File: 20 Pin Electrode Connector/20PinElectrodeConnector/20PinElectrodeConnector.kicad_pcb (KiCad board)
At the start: 2 copper layers, 21 parts, among them J1 Conn_02x10_Odd_Even

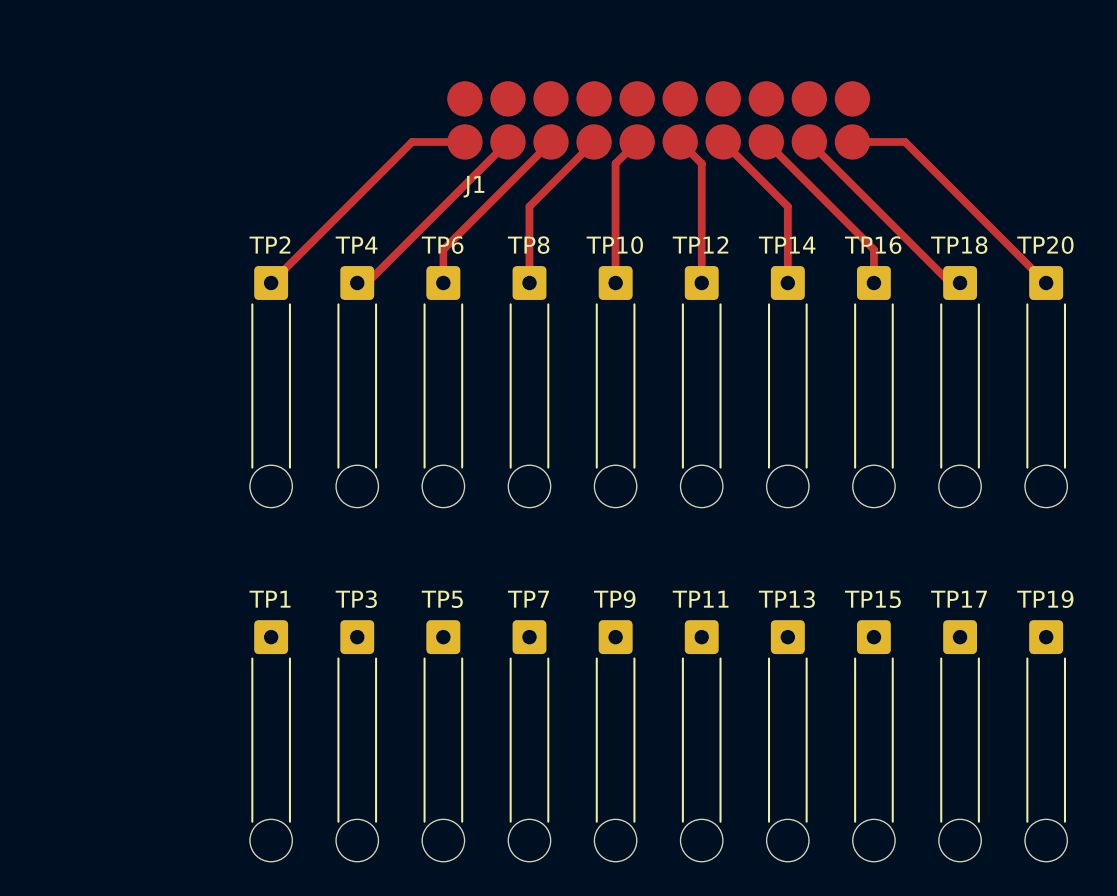
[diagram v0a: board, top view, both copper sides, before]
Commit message: Conform to microscope stage bracket.
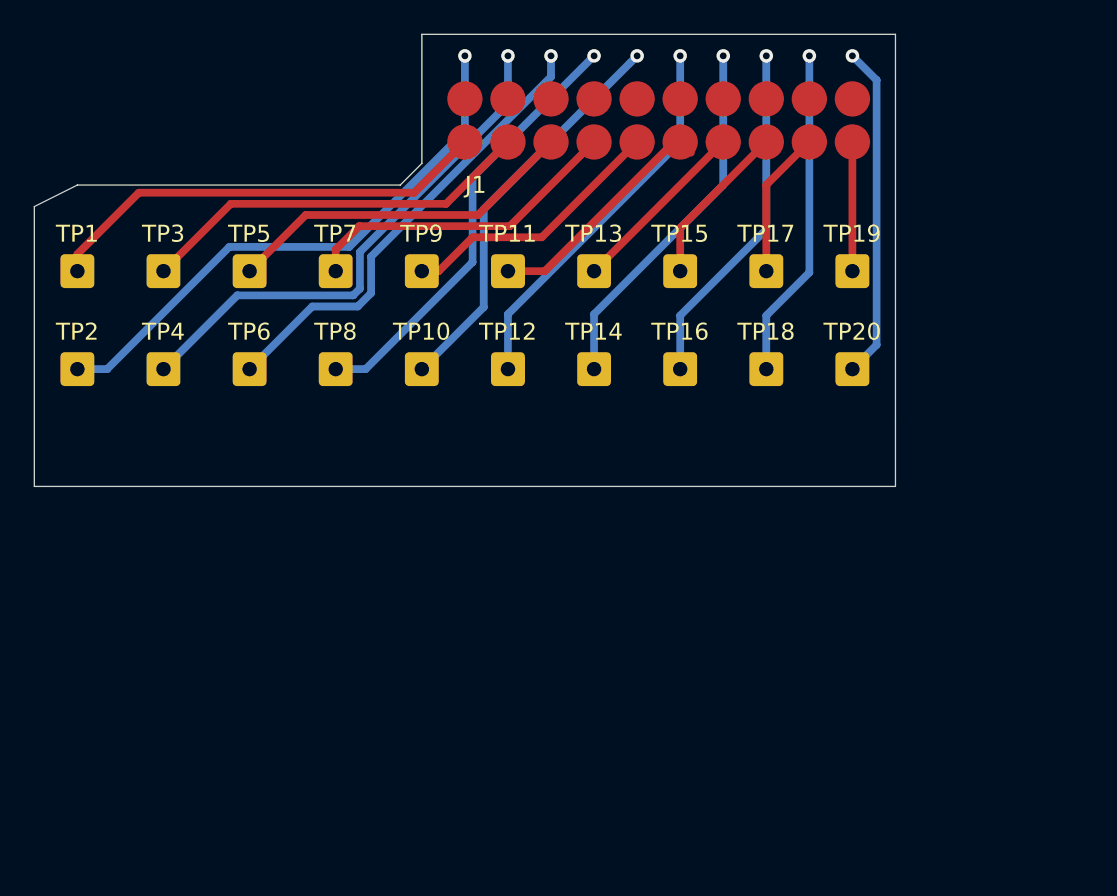
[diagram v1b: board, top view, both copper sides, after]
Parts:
- TP1, TP10, TP11, TP12, TP13, TP14, TP15, TP16, TP17, TP18, TP19, TP2, TP20, TP3, TP4, TP5, TP6, TP7, TP8, TP9: footprint Connector_Wire:SolderWire-0.25sqmm_1x01_D0.65mm_OD2mm_Relief -> Connector_Wire:SolderWire-0.25sqmm_1x01_D0.65mm_OD2mm
- moved TP11 24.4 mm to (114.3, 73.7)
- moved TP13 24.4 mm to (119.4, 73.7)
- moved TP17 24.4 mm to (129.5, 73.7)
- moved TP19 24.4 mm to (134.6, 73.7)
- moved TP9 24.4 mm to (109.2, 73.7)
- moved TP1 24.4 mm to (88.9, 73.7)
- moved TP15 24.4 mm to (124.5, 73.7)
- moved TP3 24.4 mm to (94.0, 73.7)
- moved TP5 24.4 mm to (99.1, 73.7)
- moved TP7 24.4 mm to (104.1, 73.7)
- moved TP10 12.5 mm to (109.2, 79.4)
- moved TP12 12.5 mm to (114.3, 79.4)
- moved TP14 12.5 mm to (119.4, 79.4)
- moved TP18 12.5 mm to (129.5, 79.4)
- moved TP20 12.5 mm to (134.6, 79.4)
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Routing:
- net Net-(J1-Pad1): track 0.00 -> 26.6 mm
- net Net-(J1-Pad3): track 0.00 -> 23.5 mm
- net Net-(J1-Pad5): track 0.00 -> 20.9 mm
- net Net-(J1-Pad7): track 0.00 -> 19.1 mm
- net Net-(J1-Pad4): track 12.3 -> 30.9 mm, vias 0 -> 1
- net Net-(J1-Pad2): track 14.9 -> 33.1 mm, vias 0 -> 1
- net Net-(J1-Pad6): track 11.0 -> 27.4 mm, vias 0 -> 1
- net Net-(J1-Pad9): track 0.00 -> 16.1 mm
- net Net-(J1-Pad8): track 9.90 -> 25.8 mm, vias 0 -> 1
- net Net-(J1-Pad10): track 8.85 -> 23.7 mm, vias 0 -> 1
- net Net-(J1-Pad11): track 0.00 -> 14.4 mm
- net Net-(J1-Pad12): track 8.85 -> 22.7 mm, vias 0 -> 1
- net Net-(J1-Pad14): track 9.90 -> 21.6 mm, vias 0 -> 1
- net Net-(J1-Pad13): track 0.00 -> 10.8 mm
- net Net-(J1-Pad15): track 0.00 -> 9.72 mm
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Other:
- board outline added: 50.8 x 26.7 mm
